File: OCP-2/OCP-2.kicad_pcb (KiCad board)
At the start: 2 copper layers, 3 parts

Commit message: обвес питания МК и ETH
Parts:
- added C1: Конденсатор*10мкФ*16В*0805, N_RLC:Конденсатор_SMD_IEC_0805, F.Cu at (160.5, 88.8)
- added C10: Конденсатор*10мкФ*16В*0805, N_RLC:Конденсатор_SMD_IEC_0805, F.Cu at (135.0, 63.5)
- added C11: Конденсатор*10мкФ*16В*0805, N_RLC:Конденсатор_SMD_IEC_0805, F.Cu at (135.0, 66.7)
- added C12: Конденсатор*0,1мкФ*25В*0603, N_RLC:Конденсатор_SMD_IEC_0603, F.Cu at (134.8, 69.6)
- added C2: Конденсатор*0,1мкФ*25В*0603, N_RLC:Конденсатор_SMD_IEC_0603, F.Cu at (161.1, 91.7)
- added C3: Конденсатор*0,1мкФ*25В*0603, N_RLC:Конденсатор_SMD_IEC_0603, F.Cu at (168.3, 88.5)
- added C4: Конденсатор*0,1мкФ*25В*0603, N_RLC:Конденсатор_SMD_IEC_0603, F.Cu at (161.1, 94.5)
- added C5: Конденсатор*0,1мкФ*25В*0603, N_RLC:Конденсатор_SMD_IEC_0603, F.Cu at (167.6, 91.7)
- added C6: Конденсатор*0,1мкФ*25В*0603, N_RLC:Конденсатор_SMD_IEC_0603, F.Cu at (167.6, 94.5)
- added C7: Конденсатор*10мкФ*16В*0805, N_RLC:Конденсатор_SMD_IEC_0805, F.Cu at (127.8, 63.5)
- added C8: Конденсатор*10мкФ*16В*0805, N_RLC:Конденсатор_SMD_IEC_0805, F.Cu at (127.8, 66.7)
- added C9: Конденсатор*0,1мкФ*25В*0603, N_RLC:Конденсатор_SMD_IEC_0603, F.Cu at (128.3, 69.6)
- added R1: Резистор*10кОм*0603, N_RLC:Резистор_SMD_0603_0,065_Вт_pnp, F.Cu at (127.2, 88.0)
- added R2: Резистор*10кОм*0603, N_RLC:Резистор_SMD_0603_0,065_Вт_pnp, F.Cu at (131.2, 88.0)
- added XP1: Вилка*PLD*6контактов*2ряда*вертикальная*AVR, N_X:Вилка_PLD6_вертикальная_AB, F.Cu at (172.2, 79.5)
- added XP2: Вилка*PLD*6контактов*2ряда*вертикальная*AVR, N_X:Вилка_PLD6_вертикальная_AB, F.Cu at (172.0, 71.5)
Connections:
- DD1 pad 15: Net-(DD1-Pad15) -> /MOSI.M
- DD1 pad 16: Net-(DD1-Pad16) -> /MISO.M
- DD1 pad 17: Net-(DD1-Pad17) -> /SCK.M
- DD1 pad 18: Net-(DD1-Pad18) -> 3V3
- DD1 pad 21: Net-(DD1-Pad21) -> GND
- DD1 pad 29: Net-(DD1-Pad29) -> /RES.M
- DD1 pad 3: Net-(DD1-Pad3) -> GND
- DD1 pad 4: Net-(DD1-Pad4) -> 3V3
- DD1 pad 5: Net-(DD1-Pad5) -> GND
- DD1 pad 6: Net-(DD1-Pad6) -> 3V3
- DD2 pad 15: Net-(DD2-Pad15) -> /MOSI.S
- DD2 pad 16: Net-(DD2-Pad16) -> /MISO.S
- DD2 pad 17: Net-(DD2-Pad17) -> /SCK.S
- DD2 pad 18: Net-(DD2-Pad18) -> 3V3
- DD2 pad 21: Net-(DD2-Pad21) -> GND
- DD2 pad 29: Net-(DD2-Pad29) -> /RES.S
- DD2 pad 3: Net-(DD2-Pad3) -> GND
- DD2 pad 4: Net-(DD2-Pad4) -> 3V3
- DD2 pad 5: Net-(DD2-Pad5) -> GND
- DD2 pad 6: Net-(DD2-Pad6) -> 3V3
- DD3 pad 1: Net-(DD3-Pad1) -> /EXR.CAP
- DD3 pad 11: Net-(DD3-Pad11) -> GND
- DD3 pad 15: Net-(DD3-Pad15) -> 3V3
- DD3 pad 18: Net-(DD3-Pad18) -> GND
- DD3 pad 19: Net-(DD3-Pad19) -> 3V3
- DD3 pad 2: Net-(DD3-Pad2) -> GND
- DD3 pad 20: Net-(DD3-Pad20) -> 3V3
- DD3 pad 21: Net-(DD3-Pad21) -> GND
- DD3 pad 22: Net-(DD3-Pad22) -> GND
- DD3 pad 25: Net-(DD3-Pad25) -> 3V3
- DD3 pad 28: Net-(DD3-Pad28) -> 3V3

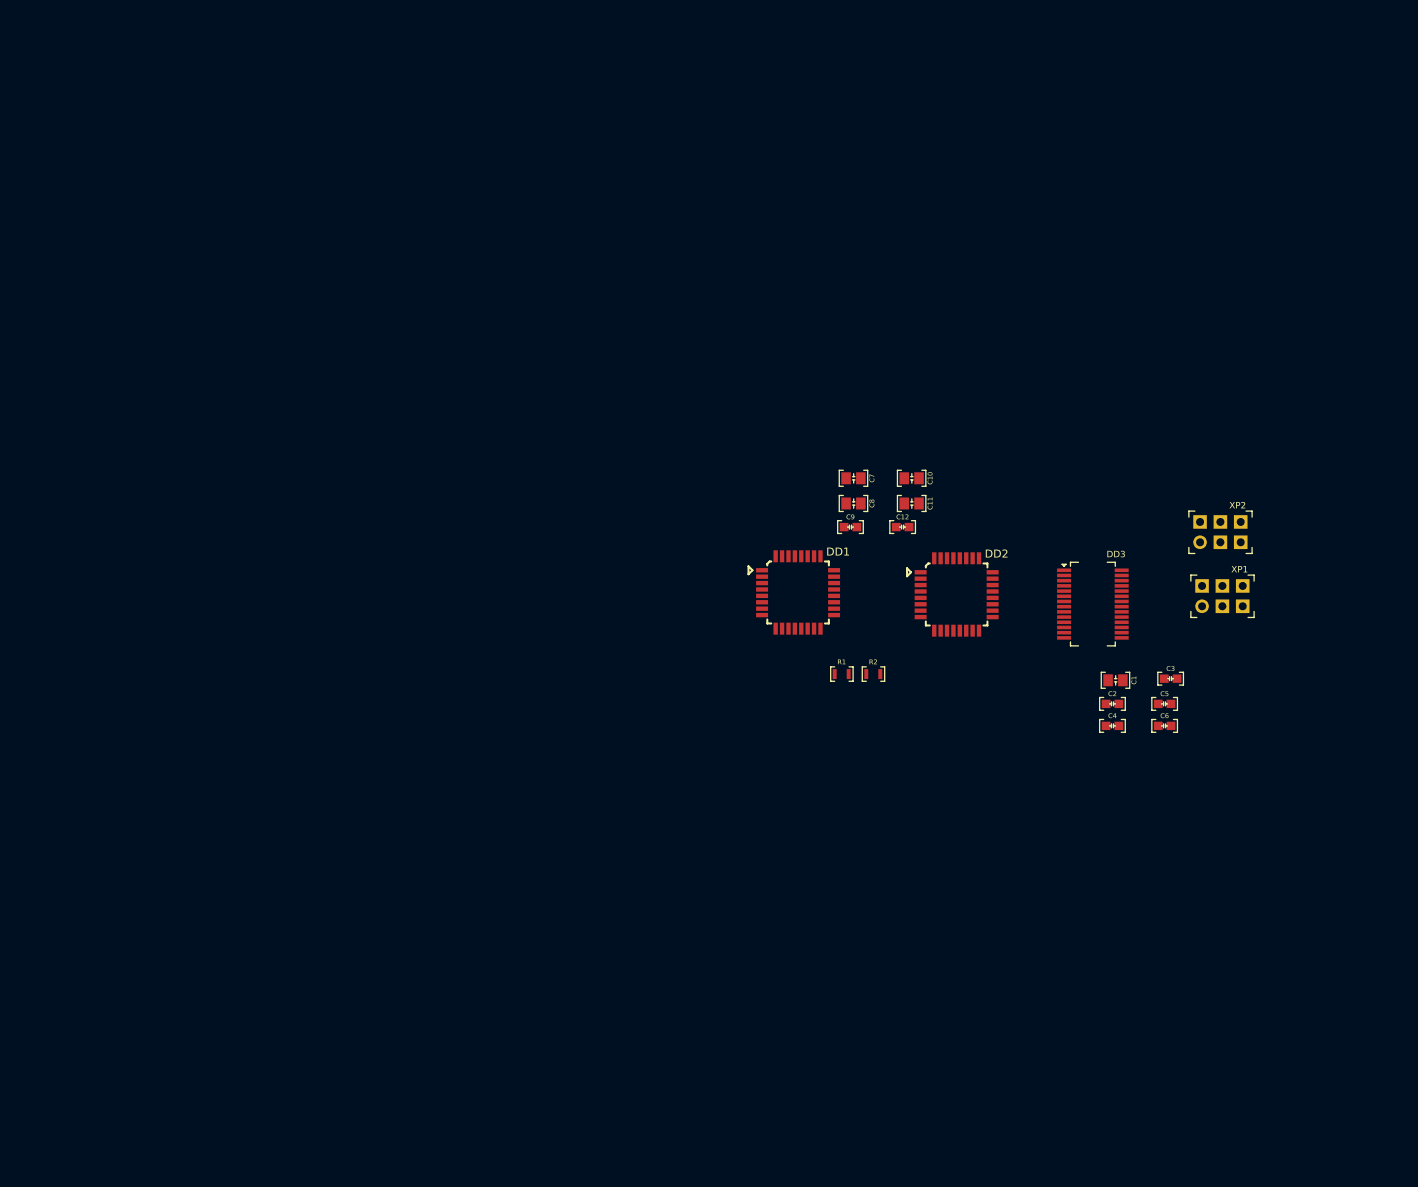
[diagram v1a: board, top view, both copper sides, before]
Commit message: схема DI и DO + трассировка
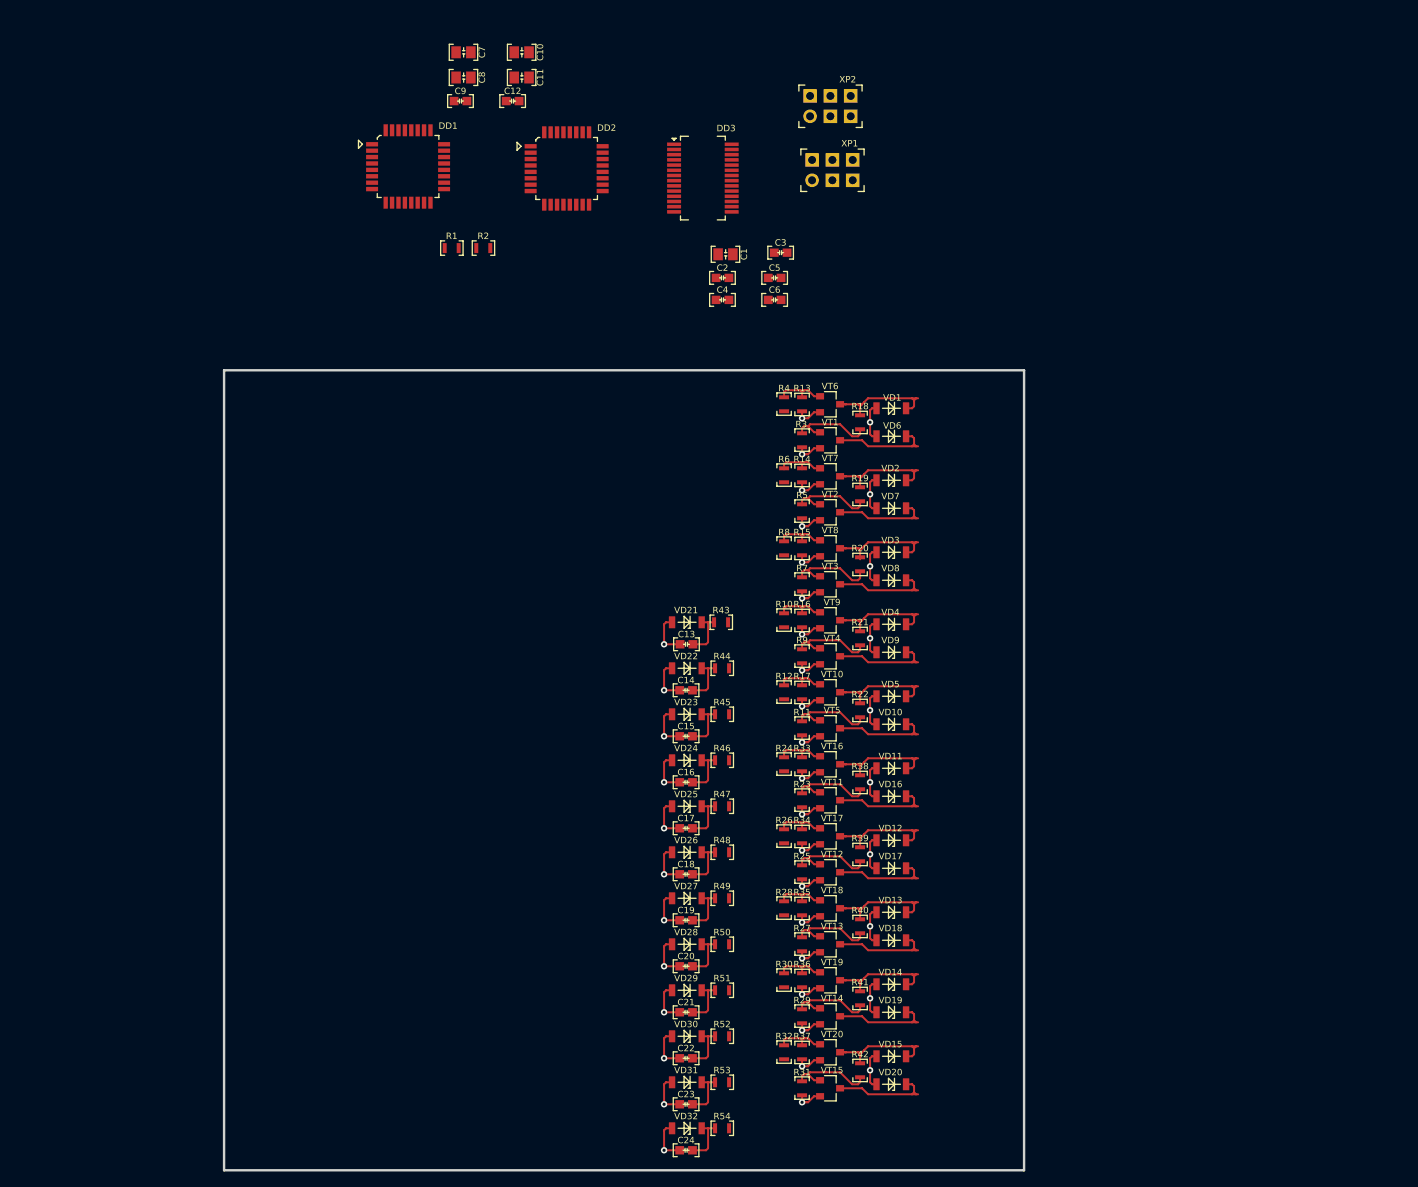
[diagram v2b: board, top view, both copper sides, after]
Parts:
- added C13: Конденсатор*0,1мкФ*25В*0603, N_RLC:Конденсатор_SMD_IEC_0603, F.Cu at (107.8, 84.2)
- added C14: Конденсатор*0,1мкФ*25В*0603, N_RLC:Конденсатор_SMD_IEC_0603, F.Cu at (107.8, 90.0)
- added C15: Конденсатор*0,1мкФ*25В*0603, N_RLC:Конденсатор_SMD_IEC_0603, F.Cu at (107.8, 95.8)
- added C16: Конденсатор*0,1мкФ*25В*0603, N_RLC:Конденсатор_SMD_IEC_0603, F.Cu at (107.8, 101.5)
- added C17: Конденсатор*0,1мкФ*25В*0603, N_RLC:Конденсатор_SMD_IEC_0603, F.Cu at (107.8, 107.2)
- added C18: Конденсатор*0,1мкФ*25В*0603, N_RLC:Конденсатор_SMD_IEC_0603, F.Cu at (107.8, 113.0)
- added C19: Конденсатор*0,1мкФ*25В*0603, N_RLC:Конденсатор_SMD_IEC_0603, F.Cu at (107.8, 118.8)
- added C20: Конденсатор*0,1мкФ*25В*0603, N_RLC:Конденсатор_SMD_IEC_0603, F.Cu at (107.8, 124.5)
- added C21: Конденсатор*0,1мкФ*25В*0603, N_RLC:Конденсатор_SMD_IEC_0603, F.Cu at (107.8, 130.2)
- added C22: Конденсатор*0,1мкФ*25В*0603, N_RLC:Конденсатор_SMD_IEC_0603, F.Cu at (107.8, 136.0)
- added C23: Конденсатор*0,1мкФ*25В*0603, N_RLC:Конденсатор_SMD_IEC_0603, F.Cu at (107.8, 141.8)
- added C24: Конденсатор*0,1мкФ*25В*0603, N_RLC:Конденсатор_SMD_IEC_0603, F.Cu at (107.8, 147.5)
- added R10: Резистор*1кОм*0603, N_RLC:Резистор_SMD_0603_0,065_Вт_pnp, F.Cu at (120.0, 81.2)
- added R11: Резистор*10кОм*0603, N_RLC:Резистор_SMD_0603_0,065_Вт_pnp, F.Cu at (122.2, 94.8)
- added R12: Резистор*1кОм*0603, N_RLC:Резистор_SMD_0603_0,065_Вт_pnp, F.Cu at (120.0, 90.2)
- added R13: Резистор*10кОм*0603, N_RLC:Резистор_SMD_0603_0,065_Вт_pnp, F.Cu at (122.2, 54.2)
- added R14: Резистор*10кОм*0603, N_RLC:Резистор_SMD_0603_0,065_Вт_pnp, F.Cu at (122.2, 63.1)
- added R15: Резистор*10кОм*0603, N_RLC:Резистор_SMD_0603_0,065_Вт_pnp, F.Cu at (122.2, 72.2)
- added R16: Резистор*10кОм*0603, N_RLC:Резистор_SMD_0603_0,065_Вт_pnp, F.Cu at (122.2, 81.2)
- added R17: Резистор*10кОм*0603, N_RLC:Резистор_SMD_0603_0,065_Вт_pnp, F.Cu at (122.2, 90.2)
- added R18: Резистор*1кОм*0603, N_RLC:Резистор_SMD_0603_0,065_Вт_pnp, F.Cu at (129.5, 56.5)
- added R19: Резистор*1кОм*0603, N_RLC:Резистор_SMD_0603_0,065_Вт_pnp, F.Cu at (129.5, 65.5)
- added R20: Резистор*1кОм*0603, N_RLC:Резистор_SMD_0603_0,065_Вт_pnp, F.Cu at (129.5, 74.2)
- added R21: Резистор*1кОм*0603, N_RLC:Резистор_SMD_0603_0,065_Вт_pnp, F.Cu at (129.5, 83.5)
- added R22: Резистор*1кОм*0603, N_RLC:Резистор_SMD_0603_0,065_Вт_pnp, F.Cu at (129.5, 92.5)
- added R23: Резистор*10кОм*0603, N_RLC:Резистор_SMD_0603_0,065_Вт_pnp, F.Cu at (122.2, 103.8)
- added R24: Резистор*1кОм*0603, N_RLC:Резистор_SMD_0603_0,065_Вт_pnp, F.Cu at (120.0, 99.2)
- added R25: Резистор*10кОм*0603, N_RLC:Резистор_SMD_0603_0,065_Вт_pnp, F.Cu at (122.2, 112.8)
- added R26: Резистор*1кОм*0603, N_RLC:Резистор_SMD_0603_0,065_Вт_pnp, F.Cu at (120.0, 108.2)
- added R27: Резистор*10кОм*0603, N_RLC:Резистор_SMD_0603_0,065_Вт_pnp, F.Cu at (122.2, 121.8)
- added R28: Резистор*1кОм*0603, N_RLC:Резистор_SMD_0603_0,065_Вт_pnp, F.Cu at (120.0, 117.2)
- added R29: Резистор*10кОм*0603, N_RLC:Резистор_SMD_0603_0,065_Вт_pnp, F.Cu at (122.2, 130.8)
- added R3: Резистор*10кОм*0603, N_RLC:Резистор_SMD_0603_0,065_Вт_pnp, F.Cu at (122.2, 58.8)
- added R30: Резистор*1кОм*0603, N_RLC:Резистор_SMD_0603_0,065_Вт_pnp, F.Cu at (120.0, 126.2)
- added R31: Резистор*10кОм*0603, N_RLC:Резистор_SMD_0603_0,065_Вт_pnp, F.Cu at (122.2, 139.8)
- added R32: Резистор*1кОм*0603, N_RLC:Резистор_SMD_0603_0,065_Вт_pnp, F.Cu at (120.0, 135.2)
- added R33: Резистор*10кОм*0603, N_RLC:Резистор_SMD_0603_0,065_Вт_pnp, F.Cu at (122.2, 99.2)
- added R34: Резистор*10кОм*0603, N_RLC:Резистор_SMD_0603_0,065_Вт_pnp, F.Cu at (122.2, 108.2)
- added R35: Резистор*10кОм*0603, N_RLC:Резистор_SMD_0603_0,065_Вт_pnp, F.Cu at (122.2, 117.2)
- added R36: Резистор*10кОм*0603, N_RLC:Резистор_SMD_0603_0,065_Вт_pnp, F.Cu at (122.2, 126.2)
- added R37: Резистор*10кОм*0603, N_RLC:Резистор_SMD_0603_0,065_Вт_pnp, F.Cu at (122.2, 135.2)
- added R38: Резистор*1кОм*0603, N_RLC:Резистор_SMD_0603_0,065_Вт_pnp, F.Cu at (129.5, 101.5)
- added R39: Резистор*1кОм*0603, N_RLC:Резистор_SMD_0603_0,065_Вт_pnp, F.Cu at (129.5, 110.5)
- added R4: Резистор*1кОм*0603, N_RLC:Резистор_SMD_0603_0,065_Вт_pnp, F.Cu at (120.0, 54.2)
- added R40: Резистор*1кОм*0603, N_RLC:Резистор_SMD_0603_0,065_Вт_pnp, F.Cu at (129.5, 119.5)
- added R41: Резистор*1кОм*0603, N_RLC:Резистор_SMD_0603_0,065_Вт_pnp, F.Cu at (129.5, 128.5)
- added R42: Резистор*1кОм*0603, N_RLC:Резистор_SMD_0603_0,065_Вт_pnp, F.Cu at (129.5, 137.5)
- added R43: Резистор*1кОм*0603, N_RLC:Резистор_SMD_0603_0,065_Вт_pnp, F.Cu at (112.1, 81.5)
- added R44: Резистор*1кОм*0603, N_RLC:Резистор_SMD_0603_0,065_Вт_pnp, F.Cu at (112.2, 87.2)
- added R45: Резистор*1кОм*0603, N_RLC:Резистор_SMD_0603_0,065_Вт_pnp, F.Cu at (112.2, 93.0)
- added R46: Резистор*1кОм*0603, N_RLC:Резистор_SMD_0603_0,065_Вт_pnp, F.Cu at (112.2, 98.8)
- added R47: Резистор*1кОм*0603, N_RLC:Резистор_SMD_0603_0,065_Вт_pnp, F.Cu at (112.2, 104.5)
- added R48: Резистор*1кОм*0603, N_RLC:Резистор_SMD_0603_0,065_Вт_pnp, F.Cu at (112.2, 110.2)
- added R49: Резистор*1кОм*0603, N_RLC:Резистор_SMD_0603_0,065_Вт_pnp, F.Cu at (112.2, 116.0)
- added R5: Резистор*10кОм*0603, N_RLC:Резистор_SMD_0603_0,065_Вт_pnp, F.Cu at (122.2, 67.6)
- added R50: Резистор*1кОм*0603, N_RLC:Резистор_SMD_0603_0,065_Вт_pnp, F.Cu at (112.2, 121.8)
- added R51: Резистор*1кОм*0603, N_RLC:Резистор_SMD_0603_0,065_Вт_pnp, F.Cu at (112.2, 127.5)
- added R52: Резистор*1кОм*0603, N_RLC:Резистор_SMD_0603_0,065_Вт_pnp, F.Cu at (112.2, 133.2)
- added R53: Резистор*1кОм*0603, N_RLC:Резистор_SMD_0603_0,065_Вт_pnp, F.Cu at (112.2, 139.0)
- added R54: Резистор*1кОм*0603, N_RLC:Резистор_SMD_0603_0,065_Вт_pnp, F.Cu at (112.2, 144.8)
- added R6: Резистор*1кОм*0603, N_RLC:Резистор_SMD_0603_0,065_Вт_pnp, F.Cu at (120.0, 63.1)
- added R7: Резистор*10кОм*0603, N_RLC:Резистор_SMD_0603_0,065_Вт_pnp, F.Cu at (122.2, 76.8)
- added R8: Резистор*1кОм*0603, N_RLC:Резистор_SMD_0603_0,065_Вт_pnp, F.Cu at (120.0, 72.2)
- added R9: Резистор*10кОм*0603, N_RLC:Резистор_SMD_0603_0,065_Вт_pnp, F.Cu at (122.2, 85.8)
- added VD1: Стабилитрон*7,5В*SOD80, N_VD_HL:SOD-80, F.Cu at (131.6, 54.8)
- added VD10: Стабилитрон*7,5В*SOD80, N_VD_HL:SOD-80, F.Cu at (131.6, 94.2)
- added VD11: Стабилитрон*7,5В*SOD80, N_VD_HL:SOD-80, F.Cu at (131.6, 99.8)
- added VD12: Стабилитрон*7,5В*SOD80, N_VD_HL:SOD-80, F.Cu at (131.6, 108.8)
- added VD13: Стабилитрон*7,5В*SOD80, N_VD_HL:SOD-80, F.Cu at (131.6, 117.8)
- added VD14: Стабилитрон*7,5В*SOD80, N_VD_HL:SOD-80, F.Cu at (131.6, 126.8)
- added VD15: Стабилитрон*7,5В*SOD80, N_VD_HL:SOD-80, F.Cu at (131.6, 135.8)
- added VD16: Стабилитрон*7,5В*SOD80, N_VD_HL:SOD-80, F.Cu at (131.6, 103.2)
- added VD17: Стабилитрон*7,5В*SOD80, N_VD_HL:SOD-80, F.Cu at (131.6, 112.2)
- added VD18: Стабилитрон*7,5В*SOD80, N_VD_HL:SOD-80, F.Cu at (131.6, 121.2)
- added VD19: Стабилитрон*7,5В*SOD80, N_VD_HL:SOD-80, F.Cu at (131.6, 130.2)
- added VD2: Стабилитрон*7,5В*SOD80, N_VD_HL:SOD-80, F.Cu at (131.6, 63.8)
- added VD20: Стабилитрон*7,5В*SOD80, N_VD_HL:SOD-80, F.Cu at (131.6, 139.2)
- added VD21: Стабилитрон*3,9В*SOD80, N_VD_HL:SOD-80, F.Cu at (106.0, 81.5)
- added VD22: Стабилитрон*3,9В*SOD80, N_VD_HL:SOD-80, F.Cu at (106.0, 87.2)
- added VD23: Стабилитрон*3,9В*SOD80, N_VD_HL:SOD-80, F.Cu at (106.0, 93.0)
- added VD24: Стабилитрон*3,9В*SOD80, N_VD_HL:SOD-80, F.Cu at (106.0, 98.8)
- added VD25: Стабилитрон*3,9В*SOD80, N_VD_HL:SOD-80, F.Cu at (106.0, 104.5)
- added VD26: Стабилитрон*3,9В*SOD80, N_VD_HL:SOD-80, F.Cu at (106.0, 110.2)
- added VD27: Стабилитрон*3,9В*SOD80, N_VD_HL:SOD-80, F.Cu at (106.0, 116.0)
- added VD28: Стабилитрон*3,9В*SOD80, N_VD_HL:SOD-80, F.Cu at (106.0, 121.8)
- added VD29: Стабилитрон*3,9В*SOD80, N_VD_HL:SOD-80, F.Cu at (106.0, 127.5)
- added VD3: Стабилитрон*7,5В*SOD80, N_VD_HL:SOD-80, F.Cu at (131.6, 72.8)
- added VD30: Стабилитрон*3,9В*SOD80, N_VD_HL:SOD-80, F.Cu at (106.0, 133.2)
- added VD31: Стабилитрон*3,9В*SOD80, N_VD_HL:SOD-80, F.Cu at (106.0, 139.0)
- added VD32: Стабилитрон*3,9В*SOD80, N_VD_HL:SOD-80, F.Cu at (106.0, 144.8)
- added VD4: Стабилитрон*7,5В*SOD80, N_VD_HL:SOD-80, F.Cu at (131.6, 81.8)
- added VD5: Стабилитрон*7,5В*SOD80, N_VD_HL:SOD-80, F.Cu at (131.6, 90.8)
- added VD6: Стабилитрон*7,5В*SOD80, N_VD_HL:SOD-80, F.Cu at (131.6, 58.2)
- added VD7: Стабилитрон*7,5В*SOD80, N_VD_HL:SOD-80, F.Cu at (131.6, 67.2)
- added VD8: Стабилитрон*7,5В*SOD80, N_VD_HL:SOD-80, F.Cu at (131.6, 76.2)
- added VD9: Стабилитрон*7,5В*SOD80, N_VD_HL:SOD-80, F.Cu at (131.6, 85.2)
- added VT1: Транзистор*pnp*0,5А*45В*SOT23, MOTOR_VD_VT_HL:Корпус_КТ-46, F.Cu at (125.8, 58.8)
- added VT10: Транзистор*npn*0,5А*45В*SOT23, MOTOR_VD_VT_HL:Корпус_КТ-46, F.Cu at (125.8, 90.2)
- added VT11: Транзистор*pnp*0,5А*45В*SOT23, MOTOR_VD_VT_HL:Корпус_КТ-46, F.Cu at (125.8, 103.8)
- added VT12: Транзистор*pnp*0,5А*45В*SOT23, MOTOR_VD_VT_HL:Корпус_КТ-46, F.Cu at (125.8, 112.8)
- added VT13: Транзистор*pnp*0,5А*45В*SOT23, MOTOR_VD_VT_HL:Корпус_КТ-46, F.Cu at (125.8, 121.8)
- added VT14: Транзистор*pnp*0,5А*45В*SOT23, MOTOR_VD_VT_HL:Корпус_КТ-46, F.Cu at (125.8, 130.8)
- added VT15: Транзистор*pnp*0,5А*45В*SOT23, MOTOR_VD_VT_HL:Корпус_КТ-46, F.Cu at (125.8, 139.8)
- added VT16: Транзистор*npn*0,5А*45В*SOT23, MOTOR_VD_VT_HL:Корпус_КТ-46, F.Cu at (125.8, 99.2)
- added VT17: Транзистор*npn*0,5А*45В*SOT23, MOTOR_VD_VT_HL:Корпус_КТ-46, F.Cu at (125.8, 108.2)
- added VT18: Транзистор*npn*0,5А*45В*SOT23, MOTOR_VD_VT_HL:Корпус_КТ-46, F.Cu at (125.8, 117.2)
- added VT19: Транзистор*npn*0,5А*45В*SOT23, MOTOR_VD_VT_HL:Корпус_КТ-46, F.Cu at (125.8, 126.2)
- added VT2: Транзистор*pnp*0,5А*45В*SOT23, MOTOR_VD_VT_HL:Корпус_КТ-46, F.Cu at (125.8, 67.8)
- added VT20: Транзистор*npn*0,5А*45В*SOT23, MOTOR_VD_VT_HL:Корпус_КТ-46, F.Cu at (125.8, 135.2)
- added VT3: Транзистор*pnp*0,5А*45В*SOT23, MOTOR_VD_VT_HL:Корпус_КТ-46, F.Cu at (125.8, 76.8)
- added VT4: Транзистор*pnp*0,5А*45В*SOT23, MOTOR_VD_VT_HL:Корпус_КТ-46, F.Cu at (125.8, 85.8)
- added VT5: Транзистор*pnp*0,5А*45В*SOT23, MOTOR_VD_VT_HL:Корпус_КТ-46, F.Cu at (125.8, 94.8)
- added VT6: Транзистор*npn*0,5А*45В*SOT23, MOTOR_VD_VT_HL:Корпус_КТ-46, F.Cu at (125.8, 54.2)
- added VT7: Транзистор*npn*0,5А*45В*SOT23, MOTOR_VD_VT_HL:Корпус_КТ-46, F.Cu at (125.8, 63.2)
- added VT8: Транзистор*npn*0,5А*45В*SOT23, MOTOR_VD_VT_HL:Корпус_КТ-46, F.Cu at (125.8, 72.2)
- added VT9: Транзистор*npn*0,5А*45В*SOT23, MOTOR_VD_VT_HL:Корпус_КТ-46, F.Cu at (125.8, 81.2)
- moved C10 72.2 mm to (86.3, 10.2)
- moved C11 72.2 mm to (86.3, 13.4)
- moved C2 72.2 mm to (112.3, 38.5)
- moved C4 72.2 mm to (112.3, 41.2)
- moved C8 72.2 mm to (79.0, 13.4)
- moved R1 72.2 mm to (78.5, 34.7)
- moved R2 72.2 mm to (82.4, 34.7)
- moved C1 72.2 mm to (111.8, 35.5)
- moved C3 72.2 mm to (119.6, 35.3)
- moved C5 72.2 mm to (118.8, 38.5)
- moved C6 72.2 mm to (118.8, 41.2)
- moved C7 72.2 mm to (79.0, 10.2)
- moved C9 72.2 mm to (79.5, 16.4)
- moved DD1 72.2 mm to (68.8, 21.8)
- moved DD2 72.2 mm to (88.6, 22.0)
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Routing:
- net GND: track 0.00 -> 149.3 mm, vias 0 -> 32
- net 5V: track 0.00 -> 39.4 mm, vias 0 -> 10
- net /DOUT3.NPN: track 0.00 -> 14.7 mm
- net /DOUT2.NPN: track 0.00 -> 14.7 mm
- net /DOUT9.NPN: track 0.00 -> 14.7 mm
- net /DOUT8.NPN: track 0.00 -> 14.7 mm
- net /DOUT7.NPN: track 0.00 -> 14.7 mm
- net /DOUT6.NPN: track 0.00 -> 14.7 mm
- net /DOUT5.NPN: track 0.00 -> 14.7 mm
- net /DOUT4.NPN: track 0.00 -> 14.7 mm
- net /DOUT10.NPN: track 0.00 -> 14.7 mm
- net /DOUT1.NPN: track 0.00 -> 14.7 mm
- net /DOUT9.PNP: track 0.00 -> 12.6 mm
- net /DOUT8.PNP: track 0.00 -> 12.6 mm
- net /DOUT7.PNP: track 0.00 -> 12.6 mm
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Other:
- board outline added: 100 x 100 mm

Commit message: размещена угловая розетка модуля
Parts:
- added X1: ico*отверстие*М3, N_X:Отверстие_М3, F.Cu at (54.0, 54.0)
- added X2: ico*отверстие*М3, N_X:Отверстие_М3, F.Cu at (54.0, 146.0)
- added XP3: Вилка*DIN41612R*64контакта*2ряда*угловая, MOTOR_X:Вилка_СНП306-64ВП21-24-1, F.Cu at (167.8, 62.5)
- added XS1: Розетка*DIN41612R*64контакта*2ряда*угловая, MOTOR_X:Розетка_СНП306-64РП21_угловая, F.Cu at (191.8, 61.0)
